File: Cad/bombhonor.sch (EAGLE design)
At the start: 71 parts, among them CN1 HEADER4X1_2MM_SMD, CN2 TR1-01, U1 STM32F030F4

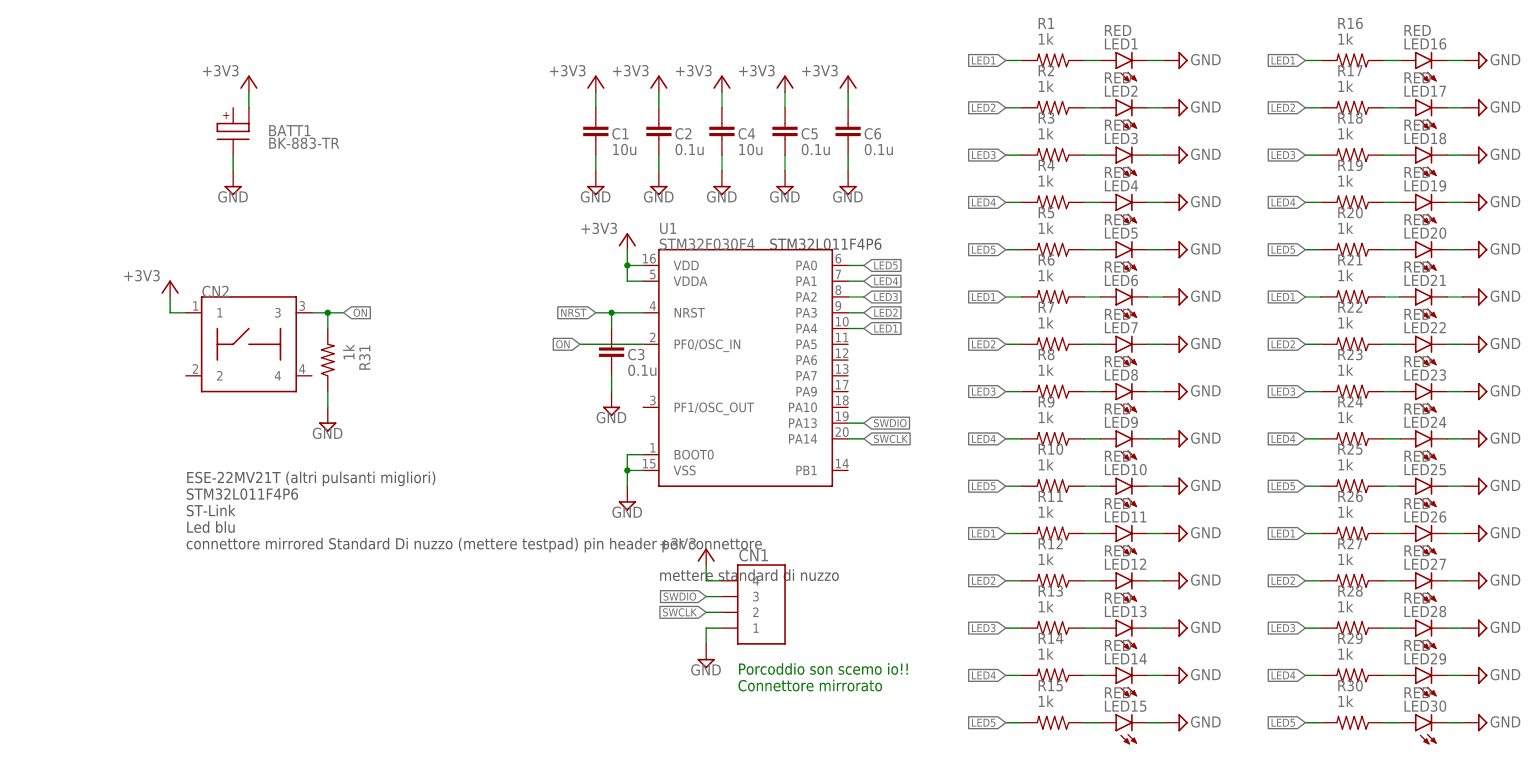
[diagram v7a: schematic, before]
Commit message: Messi i testpad sul PCB invece che il connettore Creato il primo supporto da provare a stampare
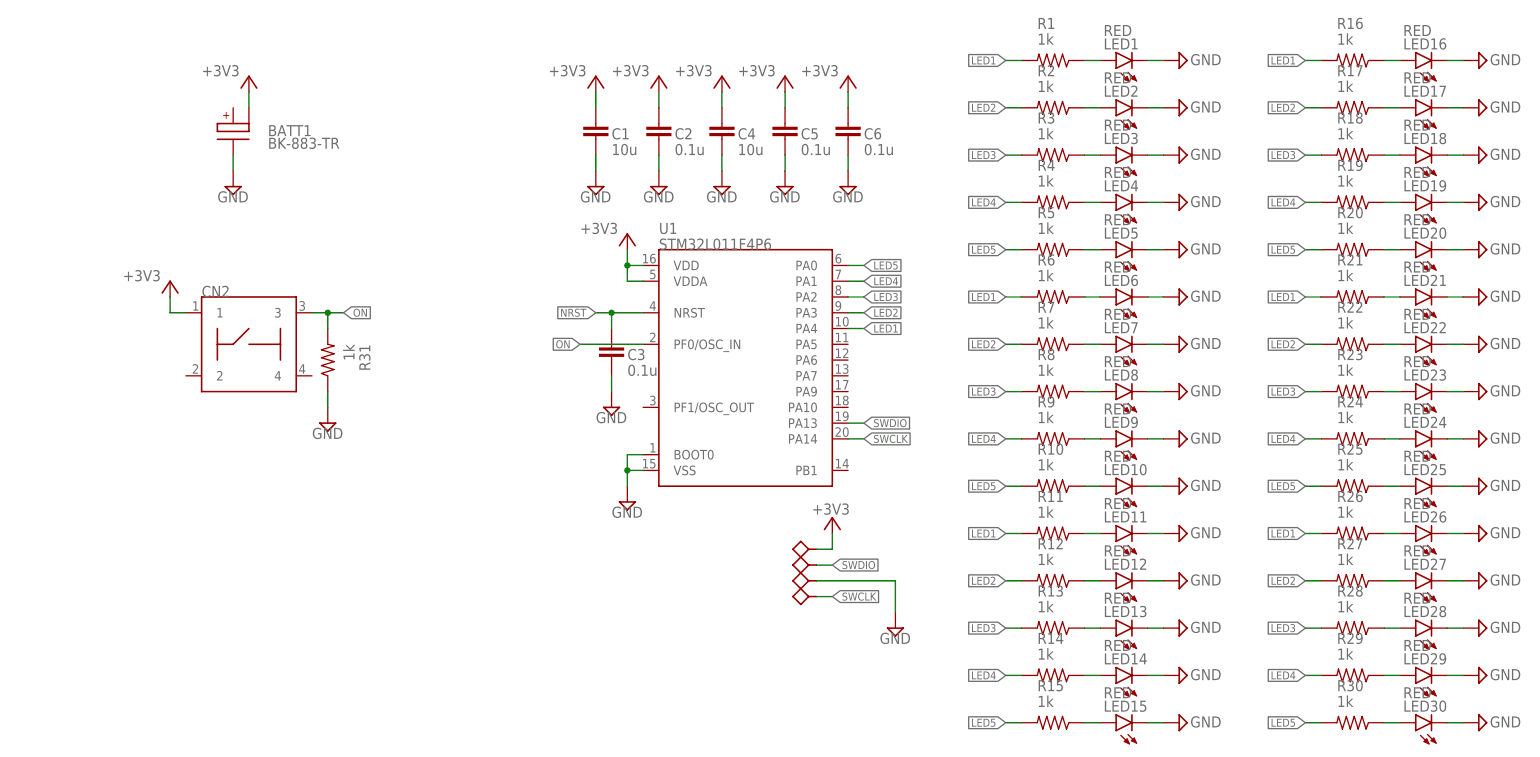
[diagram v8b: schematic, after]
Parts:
- removed CN1: HEADER4X1_2MM_SMD, AlmaCONN:HEADER4X1_2MM_SMD
- added TP1, TP2, TP3, TP4: TESTPAD2MM, AlmaCONN:TESTPAD2MM
- U1: value STM32F030F4 -> STM32L011F4P6
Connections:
- net +3V3: now also TP1.P$1; no longer CN1.4
- net GND: now also TP3.P$1; no longer CN1.1
- net SWCLK: now also TP4.P$1; no longer CN1.2
- net SWDIO: now also TP2.P$1; no longer CN1.3
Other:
- note removed: "ESE-22MV21T (altri pulsanti migliori) STM32L011F4P6 ST-Link Led blu connettore mirrored Standard Di nuzzo (mettere testpad) pin header per connettore"
- note removed: "Porcoddio son scemo io!! Connettore mirrorato"
- note removed: "STM32L011F4P6"
- note removed: "mettere standard di nuzzo"
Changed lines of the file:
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@@
 <attribute name="PARTNO" value="LTST-C230KRKT"/>
 </part>
-<part name="U1" library="AlmaIC" deviceset="STM32F030F4" device="">
+<part name="U1" library="AlmaIC" deviceset="STM32F030F4" device="" value="STM32L011F4P6">
 <attribute name="PARTNO" value="STM32L011F4P6"/>
 </part>
@@
 <part name="GND36" library="AlmaSUP" deviceset="GND" device=""/>
 <part name="GND37" library="AlmaSUP" deviceset="GND" device=""/>
-<part name="+3V7" library="AlmaSUP" deviceset="+3V3" device=""/>
-<part name="GND38" library="AlmaSUP" deviceset="GND" device=""/>
 <part name="3" library="AlmaFRAME" deviceset="FRAME_A4" device=""/>
 <part name="BATT1" library="AlmaBATT" deviceset="BK-883-TR" device="">
@@
 </part>
 <part name="GND43" library="AlmaSUP" deviceset="GND" device=""/>
-<part name="CN1" library="AlmaCONN" deviceset="HEADER4X1" device="_2MM_SMD">
-<attribute name="PARTNO" value="2PH1-04-UA-SMT-B"/>
-</part>
 <part name="CN2" library="cesso" deviceset="TR1-01" device="">
 <attribute name="PARTNO" value="TR1-01"/>
@@
 <part name="GND39" library="AlmaSUP" deviceset="GND" device=""/>
 <part name="+3V8" library="AlmaSUP" deviceset="+3V3" device=""/>
+<part name="TP1" library="AlmaCONN" deviceset="TESTPAD" device="2MM"/>
+<part name="TP2" library="AlmaCONN" deviceset="TESTPAD" device="2MM"/>
+<part name="TP3" library="AlmaCONN" deviceset="TESTPAD" device="2MM"/>
+<part name="TP4" library="AlmaCONN" deviceset="TESTPAD" device="2MM"/>
+<part name="GND40" library="AlmaSUP" deviceset="GND" device=""/>
+<part name="+3V10" library="AlmaSUP" deviceset="+3V3" device=""/>
 </parts>
 <sheets>
@@
 <description>Connectors</description>
 <plain>
-<text x="132.08" y="137.16" size="1.778" layer="97">STM32L011F4P6</text>
-<text x="114.3" y="83.82" size="1.778" layer="97">mettere standard di nuzzo</text>
-<text x="38.1" y="88.9" size="1.778" layer="97">ESE-22MV21T (altri pulsanti migliori)
-STM32L011F4P6
-ST-Link
-Led blu
-connettore mirrored Standard Di nuzzo (mettere testpad) pin header per connettore
-</text>
-<text x="127" y="66.04" size="1.778" layer="91">Porcoddio son scemo io!!
-Connettore mirrorato</text>
 </plain>
 <instances>
@@
 <attribute name="VALUE" x="142.24" y="144.78" size="1.778" layer="96"/>
 </instance>
-<instance part="+3V7" gate="G$1" x="121.92" y="88.9" smashed="yes">
-<attribute name="VALUE" x="114.3" y="88.9" size="1.778" layer="96"/>
-</instance>
-<instance part="GND38" gate="1" x="121.92" y="71.12" smashed="yes">
-<attribute name="VALUE" x="119.38" y="68.58" size="1.778" layer="96"/>
-</instance>
 <instance part="3" gate="G$1" x="0" y="0" smashed="yes">
 <attribute name="DRAWING_NAME" x="217.17" y="15.24" size="2.54" layer="94"/>
@@
 <attribute name="VALUE" x="43.18" y="144.78" size="1.778" layer="96"/>
 </instance>
-<instance part="CN1" gate="G$1" x="129.54" y="78.74" smashed="yes" rot="R180">
-<attribute name="NAME" x="132.08" y="88.9" size="1.9304" layer="95" rot="R180"/>
-<attribute name="PARTNO" x="129.54" y="78.74" size="1.778" layer="96" rot="R180" display="off"/>
-</instance>
 <instance part="CN2" gate="G$1" x="48.26" y="121.92" smashed="yes">
 <attribute name="NAME" x="40.64" y="129.54" size="1.778" layer="95"/>
@@
 <instance part="+3V8" gate="G$1" x="48.26" y="165.1" smashed="yes">
 <attribute name="VALUE" x="40.64" y="165.1" size="1.778" layer="96"/>
+</instance>
+<instance part="TP1" gate="G$1" x="139.7" y="88.9" smashed="yes" rot="R90"/>
+<instance part="TP2" gate="G$1" x="139.7" y="86.36" smashed="yes" rot="R90"/>
+<instance part="TP3" gate="G$1" x="139.7" y="83.82" smashed="yes" rot="R90"/>
+<instance part="TP4" gate="G$1" x="139.7" y="81.28" smashed="yes" rot="R90"/>
+<instance part="GND40" gate="1" x="152.4" y="76.2" smashed="yes">
+<attribute name="VALUE" x="149.86" y="73.66" size="1.778" layer="96"/>
+</instance>
+<instance part="+3V10" gate="G$1" x="142.24" y="93.98" smashed="yes">
+<attribute name="VALUE" x="138.938" y="94.488" size="1.778" layer="96"/>
 </instance>
 </instances>
@@
 </segment>
 <segment>
-<pinref part="GND38" gate="1" pin="GND"/>
-<pinref part="CN1" gate="G$1" pin="1"/>
-<wire x1="124.46" y1="76.2" x2="121.92" y2="76.2" width="0.1524" layer="91"/>
-<wire x1="121.92" y1="76.2" x2="121.92" y2="73.66" width="0.1524" layer="91"/>
-</segment>
-<segment>
 <pinref part="GND43" gate="1" pin="GND"/>
 <pinref part="BATT1" gate="G$1" pin="GND"/>
@@
 <pinref part="GND39" gate="1" pin="GND"/>
 <wire x1="60.96" y1="114.3" x2="60.96" y2="111.76" width="0.1524" layer="91"/>
+</segment>
+<segment>
+<pinref part="GND40" gate="1" pin="GND"/>
+<wire x1="139.7" y1="83.82" x2="152.4" y2="83.82" width="0.1524" layer="91"/>
+<wire x1="152.4" y1="83.82" x2="152.4" y2="78.74" width="0.1524" layer="91"/>
+<pinref part="TP3" gate="G$1" pin="P$1"/>
 </segment>
 </net>
@@
 </segment>
 <segment>
-<pinref part="+3V7" gate="G$1" pin="+3V3"/>
-<wire x1="124.46" y1="83.82" x2="121.92" y2="83.82" width="0.1524" layer="91"/>
-<wire x1="121.92" y1="83.82" x2="121.92" y2="86.36" width="0.1524" layer="91"/>
-<pinref part="CN1" gate="G$1" pin="4"/>
-</segment>
-<segment>
 <pinref part="+3V9" gate="G$1" pin="+3V3"/>
 <pinref part="CN2" gate="G$1" pin="1"/>
@@
 <wire x1="48.26" y1="162.56" x2="48.26" y2="160.02" width="0.1524" layer="91"/>
 <pinref part="BATT1" gate="G$1" pin="V_BATT2"/>
+</segment>
+<segment>
+<wire x1="139.7" y1="88.9" x2="142.24" y2="88.9" width="0.1524" layer="91"/>
+<wire x1="142.24" y1="88.9" x2="142.24" y2="91.44" width="0.1524" layer="91"/>
+<pinref part="+3V10" gate="G$1" pin="+3V3"/>
+<pinref part="TP1" gate="G$1" pin="P$1"/>
 </segment>
 </net>
@@
 </segment>
 <segment>
-<wire x1="121.92" y1="78.74" x2="124.46" y2="78.74" width="0.1524" layer="91"/>
-<label x="121.92" y="78.74" size="1.27" layer="95" rot="R180" xref="yes"/>
-<pinref part="CN1" gate="G$1" pin="2"/>
+<wire x1="142.24" y1="81.28" x2="139.7" y2="81.28" width="0.1524" layer="91"/>
+<label x="142.24" y="81.28" size="1.27" layer="95" xref="yes"/>
+<pinref part="TP4" gate="G$1" pin="P$1"/>
 </segment>
 </net>
@@
 </segment>
 <segment>
-<wire x1="121.92" y1="81.28" x2="124.46" y2="81.28" width="0.1524" layer="91"/>
-<label x="121.92" y="81.28" size="1.27" layer="95" rot="R180" xref="yes"/>
-<pinref part="CN1" gate="G$1" pin="3"/>
+<wire x1="142.24" y1="86.36" x2="139.7" y2="86.36" width="0.1524" layer="91"/>
+<label x="142.24" y="86.36" size="1.27" layer="95" xref="yes"/>
+<pinref part="TP2" gate="G$1" pin="P$1"/>
 </segment>
 </net>
@@
 </schematic>
 </drawing>
-<compatibility>
-<note version="6.3" minversion="6.2.2" severity="warning">
-Since Version 6.2.2 text objects can contain more than one line,
-which will not be processed correctly with this version.
-</note>
-</compatibility>
 </eagle>
